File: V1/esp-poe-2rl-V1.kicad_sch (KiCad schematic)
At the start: 72 parts, among them J1 USB_C_Receptacle_USB2.0, J2 250-202, J3 RJ45 JACK, J4 250-202, K1 G5NB-1A-E-DC5, K2 G5NB-1A-E-DC5, Q1 UMH3N, Q2 MMBT2222A, Q3 WPM2015-3/TR, Q4 LMUN2211LT1G, Q5 MMBT2222A, SW1 RESET, U1 CH340K, U2 ESP32-WROOM-32UE-N16, U3 LAN8710A

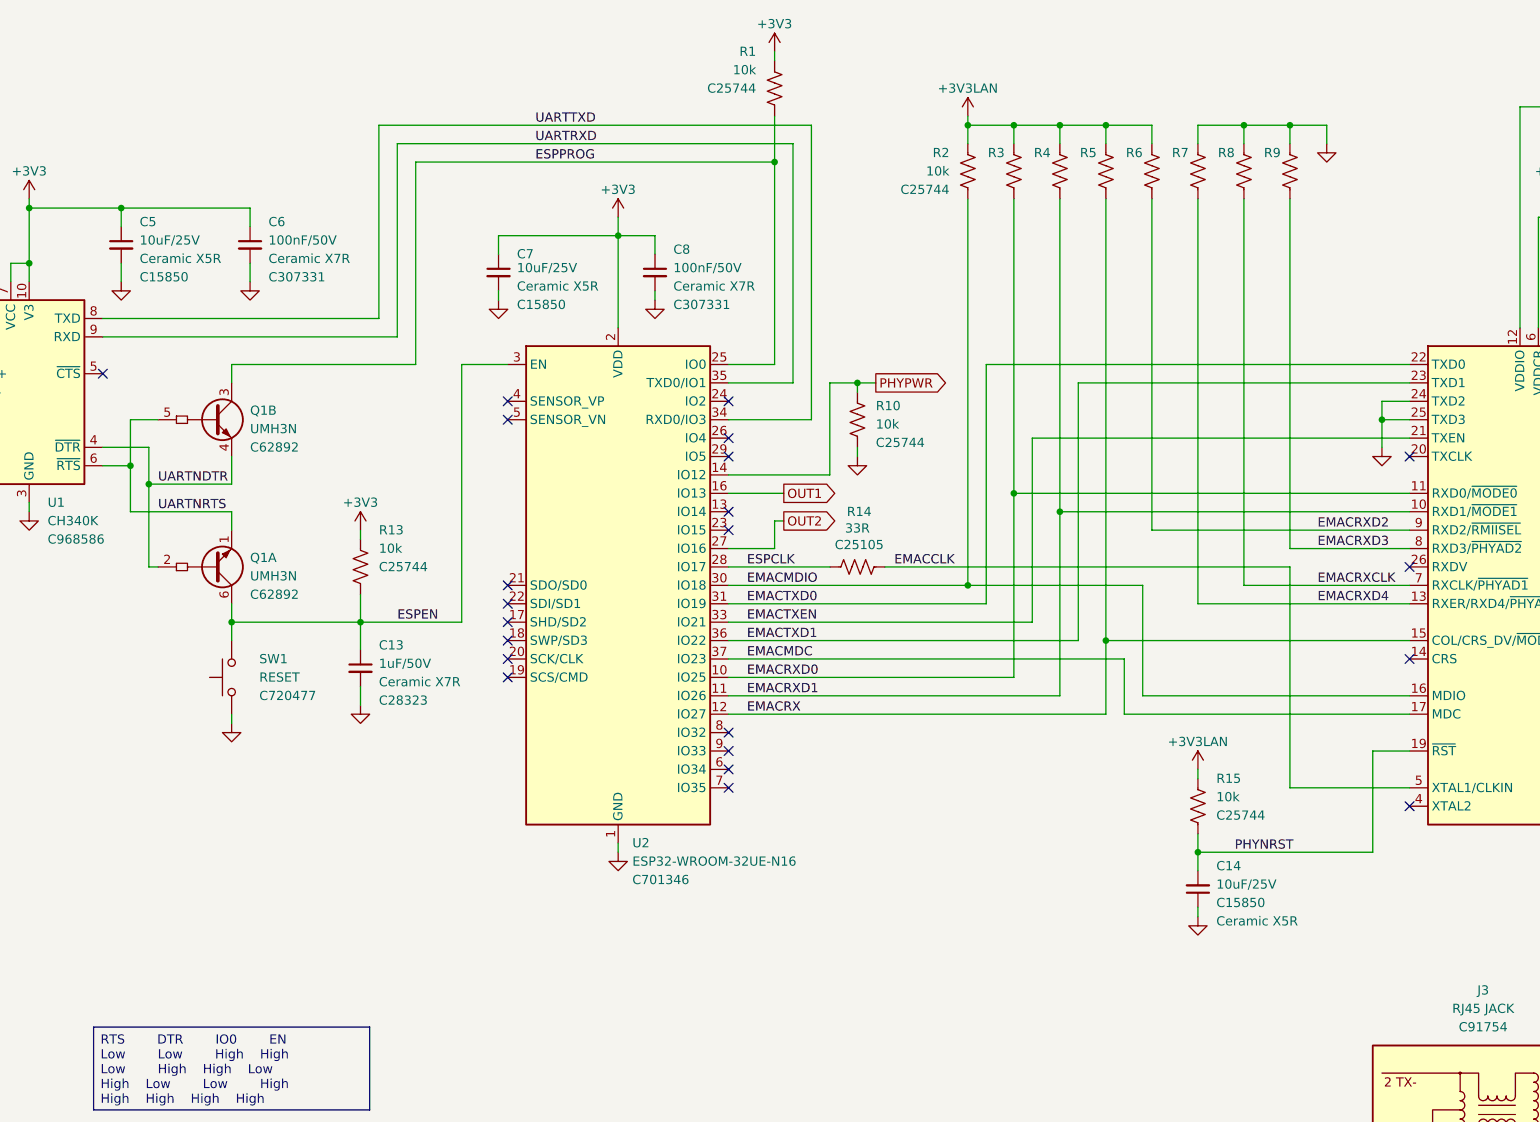
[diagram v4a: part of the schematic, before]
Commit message: Update resistance value for pull-ups.
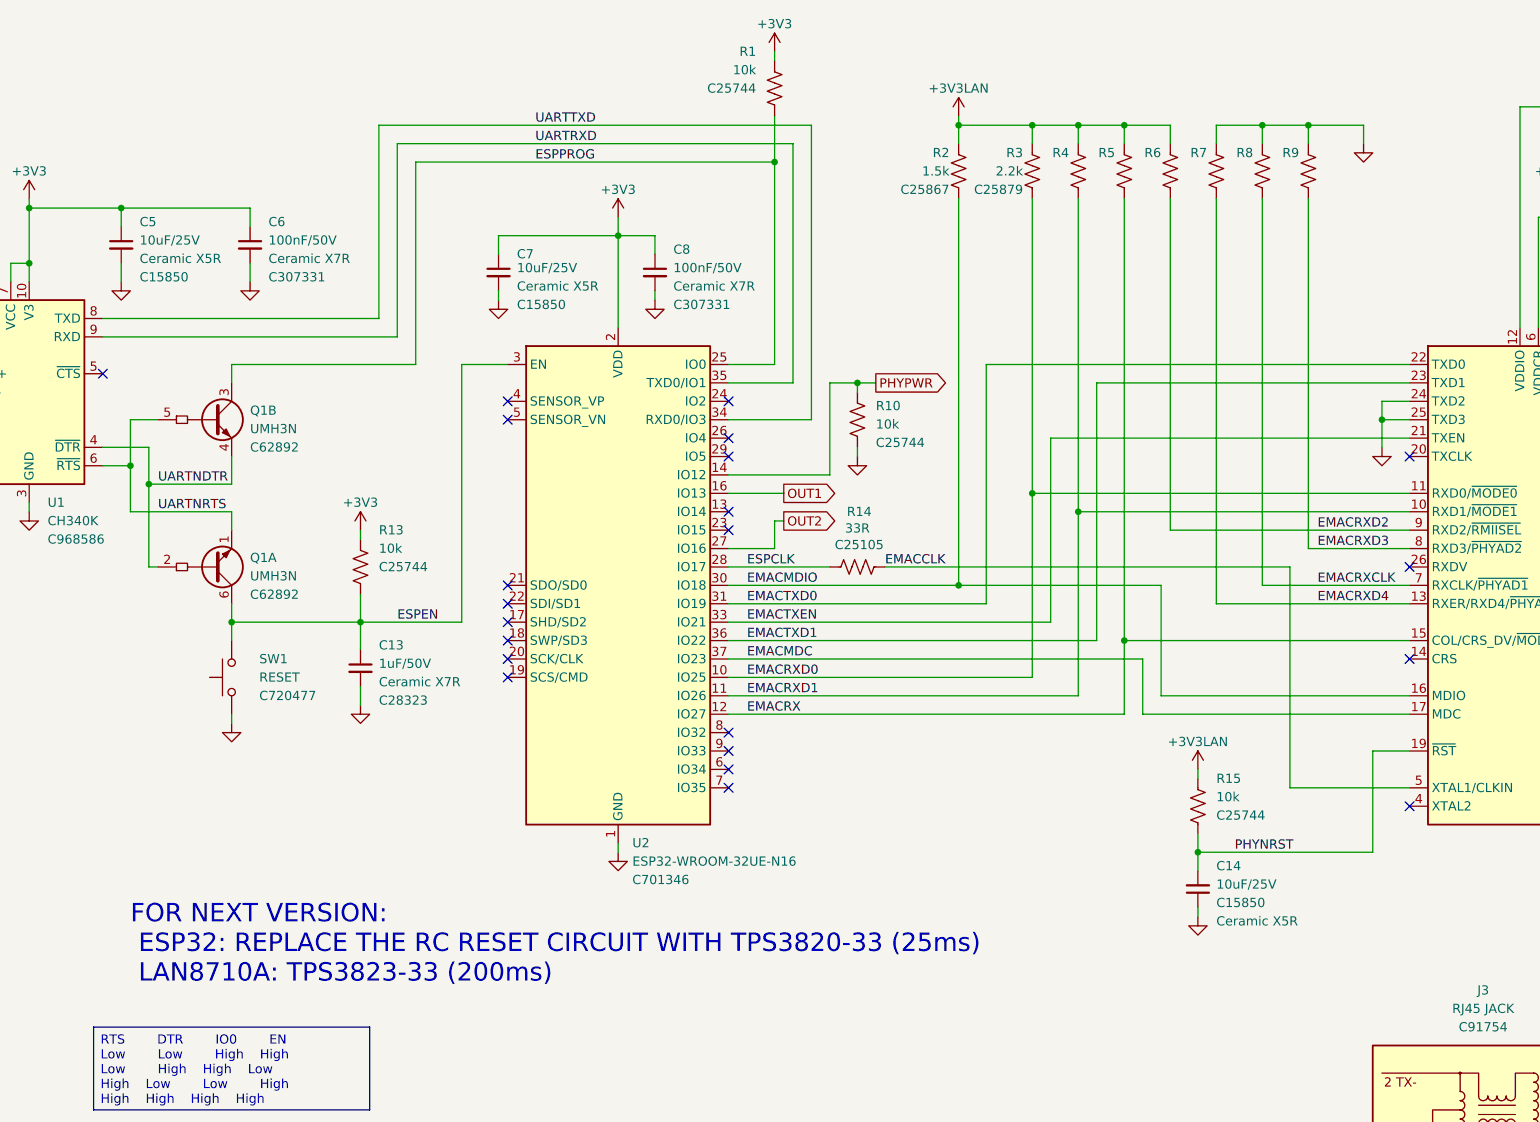
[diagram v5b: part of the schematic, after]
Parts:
- R2: value 10k -> 1.5k; LCSC Part # C25744 -> C25867; Mfr PN 0402WGF1002TCE -> 0402WGF1501TCE; Vendor PN C25744 -> C25867
- R3, R4, R5, R6, R7, R8, R9: value 10k -> 2.2k; LCSC Part # C25744 -> C25879; Mfr PN 0402WGF1002TCE -> 0402WGF2201TCE; Vendor PN C25744 -> C25879
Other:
- note added: "FOR NEXT VERSION: ESP32: REPLACE THE RC RESET CIRCUIT WITH TPS3820-33 (25ms) LAN8710A: TPS3823-33 (200ms)"
- moved on the sheet: R2, R3, R4, R5, R6, R7, R8, R9

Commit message: Revising before manufacture
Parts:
- removed D3, D5: 1N4148, Tales:D_SOD-123, symbol Diode:1N4148
- removed D4, D6: WHITE, Tales:LED_0603_1608Metric, symbol Device:LED_Small
- removed J2, J4: 250-202, Tales:TerminalBlock_Wago_250-202_1x02_P3.5mm_45Degree, symbol Connector_Generic:Conn_01x02
- removed K1, K2: G5NB-1A-E-DC5, Tales:Relay_SPST_Omron_G5NB-1A, symbol Tales:G5NB-1A
- removed Q2, Q5: MMBT2222A, Tales:SOT-23, symbol Transistor_BJT:Q_NPN_BEC
- removed R21, R27: 680R, Tales:R_0402_1005Metric, symbol Device:R_US
- removed R22, R29: 1k, Tales:R_0402_1005Metric, symbol Device:R_US
- removed R23, R30: 10k, Tales:R_0402_1005Metric, symbol Device:R_US
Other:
- added sheet RELAY OUTPUTS (esp-poe-2rl-v1-outputs.kicad_sch)
- sheet POWER: file esp-poe-2rl-V1-power.kicad_sch -> esp-poe-2rl-v1-power.kicad_sch
- moved on the sheet: C16, C17, C18, C19, L1, Q3, Q4, R14, R25, R28

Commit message: V1.4.0
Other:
- note added: "MODE[2:0]=111 ALL CAPABLE AUTONEG ENABLED"
- note added: "PHYAD[2:0]=000 PHY ADRESS 0X00"
- note added: "RMIISEL=1 RMII MODE"
- moved on the sheet: C13, C7, C8, R1, R10, R13, R14, U2
